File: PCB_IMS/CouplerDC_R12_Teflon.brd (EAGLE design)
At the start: 104.4 x 48.3 mm, 61 parts

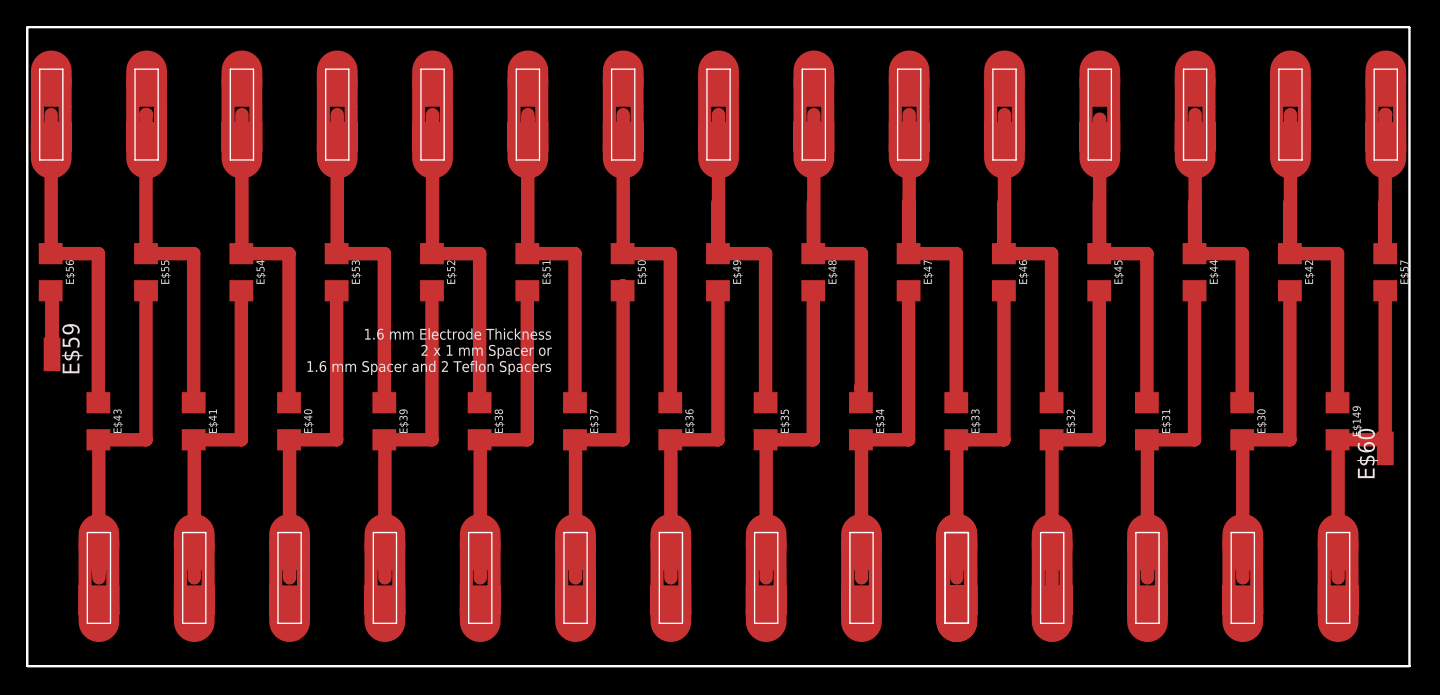
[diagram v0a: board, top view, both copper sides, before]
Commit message: Added smaller electrode board and spacers
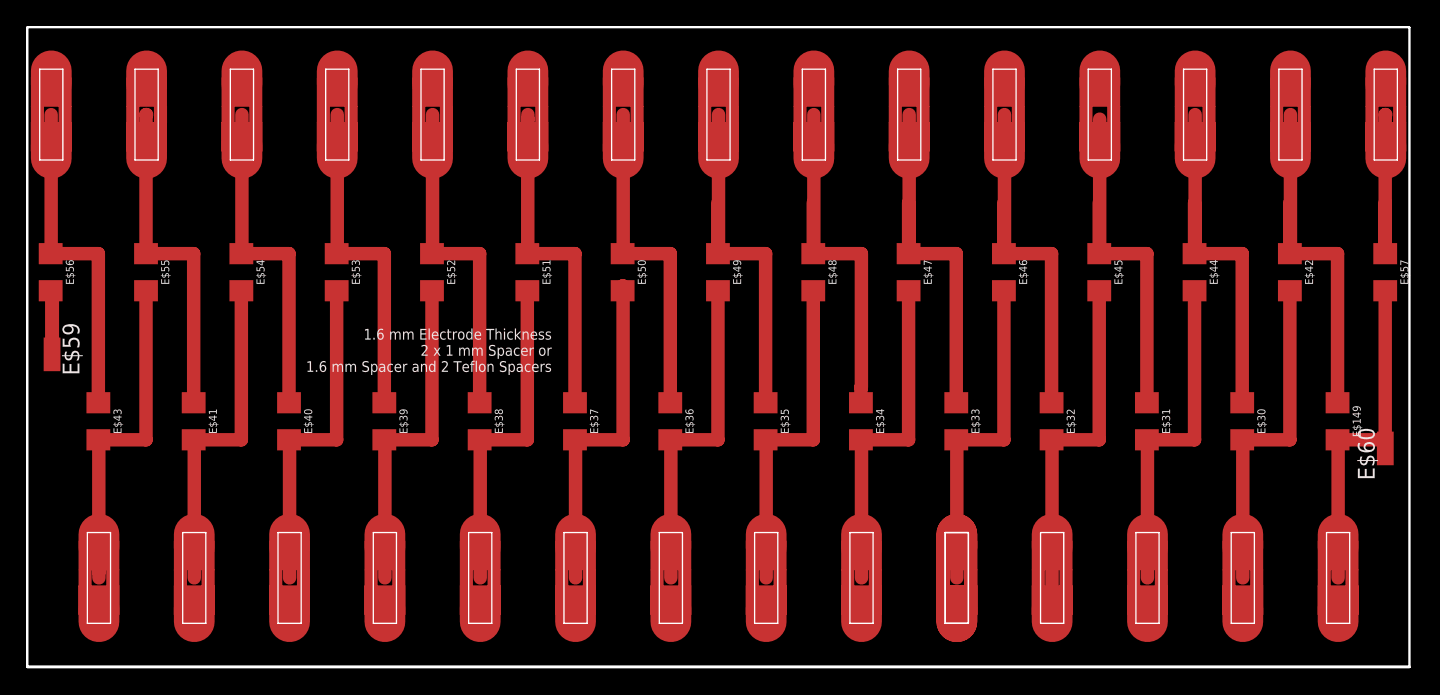
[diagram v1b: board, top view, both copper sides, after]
